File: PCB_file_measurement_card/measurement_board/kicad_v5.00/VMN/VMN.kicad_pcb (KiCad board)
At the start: 2 copper layers, 210.8 x 86.4 mm, 53 parts, among them J1 A/B, J10 Conn_01x08_Female, J11 Conn_01x02_Female, J12 Conn_01x02_Female, J13 Conn_01x08_Female, J2 Screw_Terminal_VMN, J3 Alim DPH5005, J4 Conn_01x08_Female, J5 Conn_01x04_Female, J6 Conn_01x08_Female, J7 Raspberry_Pi_2_3, J8 Conn_02x03_Top_Bottom, J9 Screw_Terminal_01x02, K1 AQY211EH, K2 AQY211EH, K3 AQY211EH, K4 AQY211EH, U1 INA128, U2 MCP23008-xP, U3 LM358, U5 1085-Adress=0X49, U6 1085-Adress=0X48

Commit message: new measurement board
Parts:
- removed Alim_5V_Digital_rasp_iso1540_mcp1, Alim_5V_ina282_iso1: THD_15-1211N, THD_15-1211N:THD151211N
- removed Alim_analog_Vmn1: THD_15-1222N, THD_15-1222N:CONV_THD_15-1222N
- removed J10: Conn_01x08_Female, Connector_PinHeader_2.54mm:PinHeader_1x08_P2.54mm_Vertical
- removed REF** (x8): Hole_3.2mm_M3, MountingHole:MountingHole_3.2mm_M3_ISO7380
- removed U6: 1085-Adress=0X48, 1085:1085
- added ?: , , F.Cu at (247.7, 150.0)
- added ?: , , F.Cu at (247.7, 91.0)
- added ?: , , F.Cu at (203.0, 149.0)
- added ?: , , F.Cu at (202.0, 91.0)
- added Alim_5VA: THD_15-1211N, THD_15-1211N:THD151211N, F.Cu at (166.9, 88.0)
- added Alim_5V_Digital: THD_15-1211N, THD_15-1211N:THD151211N, F.Cu at (190.0, 93.0)
- added Alim_analog_Vmn_measurement_ina128P_lm158: THD_15-1222N, THD_15-1222N:CONV_THD_15-1222N, F.Cu at (85.0, 104.0)
- added D5: BAT86, Diode_THT:D_DO-35_SOD27_P7.62mm_Horizontal, F.Cu at (108.0, 72.2)
- added D6: BAT86, Diode_THT:D_DO-35_SOD27_P7.62mm_Horizontal, F.Cu at (104.0, 79.8)
- added D7: 1N4148, Diode_THT:D_DO-35_SOD27_P7.62mm_Horizontal, F.Cu at (48.0, 67.2)
- added D8: 1N4148, Diode_THT:D_DO-35_SOD27_P7.62mm_Horizontal, F.Cu at (48.0, 79.2)
- added J14: Conn_01x02_Female, Connector_PinHeader_2.54mm:PinHeader_1x02_P2.54mm_Vertical, F.Cu at (86.0, 128.0)
- added J15: Conn_01x08_Female, Connector_PinHeader_2.54mm:PinHeader_1x08_P2.54mm_Vertical, F.Cu at (98.0, 141.0)
- added J16: RX_bat, TerminalBlock_Phoenix:TerminalBlock_Phoenix_MKDS-1,5-2-5.08_1x02_P5.08mm_Horizontal, F.Cu at (189.5, 139.3)
- added K5: AQY212EH, AQY211EH:DIP762W47P254L478H340Q4N, F.Cu at (51.0, 135.0)
- added K6: AQY212EH, AQY211EH:DIP762W47P254L478H340Q4N, F.Cu at (51.0, 141.0)
- added Q1: ZVN4206ASTZ, Package_TO_SOT_THT:TO-92L_Inline, F.Cu at (231.0, 67.0)
- added Q2: ZVN4206ASTZ, Package_TO_SOT_THT:TO-92L_Inline, F.Cu at (208.0, 67.0)
- added R7: 1k, Resistor_THT:R_Axial_DIN0207_L6.3mm_D2.5mm_P7.62mm_Horizontal, F.Cu at (57.2, 142.0)
- added R8: 2, Resistor_THT:R_Axial_DIN0414_L11.9mm_D4.5mm_P20.32mm_Horizontal, F.Cu at (73.0, 142.2)
- added R9: 20 Mohms, Resistor_THT:R_Axial_DIN0204_L3.6mm_D1.6mm_P7.62mm_Horizontal, F.Cu at (44.0, 79.2)
- added U4: 1115-Adress=0X49, 1085:1085, F.Cu at (114.6, 87.4)
- D1, D2: value BAT86 -> 1N4001; footprint Diode_THT:D_DO-35_SOD27_P7.62mm_Horizontal -> Diode_THT:D_DO-41_SOD81_P10.16mm_Horizontal
- J1: value A/B -> DSP_out_12v_GND
- J11: value Conn_01x02_Female -> Screw_Terminal_VMN; footprint Connector_PinHeader_2.54mm:PinHeader_1x02_P2.54mm_Vertical -> TerminalBlock_Phoenix:TerminalBlock_Phoenix_MKDS-1,5-2-5.08_1x02_P5.08mm_Horizontal
- J12: value Conn_01x02_Female -> Conn_01x08_Female; footprint Connector_PinHeader_2.54mm:PinHeader_1x02_P2.54mm_Vertical -> Connector_PinHeader_2.54mm:PinHeader_1x08_P2.54mm_Vertical
- J13: value Conn_01x08_Female -> Conn_01x02_Female; footprint Connector_PinHeader_2.54mm:PinHeader_1x08_P2.54mm_Vertical -> Connector_PinHeader_2.54mm:PinHeader_1x02_P2.54mm_Vertical
- J2: value Screw_Terminal_VMN -> DPS5005_input_0_to_50V
- J3: value Alim DPH5005 -> Screw_Terminal_AB
- J4: moved to F.Cu
- J7: value Raspberry_Pi_2_3 -> Raspberry_Pi_2_3_4; moved to F.Cu
- J8: value Conn_02x03_Top_Bottom -> Connector_I2C_for_mux_or_tools
- J9: value Screw_Terminal_01x02 -> TX_bat; moved to B.Cu
- K1, K2: value AQY211EH -> G5LE-1; footprint AQY211EH:DIP762W47P254L478H340Q4N -> Relay_THT:Relay_SPDT_Omron-G5LE-1
- K3, K4: value AQY211EH -> AQY212EH
- R1, R2: value 1.5k -> 100k
- R6: value 2 -> 1k; footprint Resistor_THT:R_Axial_DIN0414_L11.9mm_D4.5mm_P20.32mm_Horizontal -> Resistor_THT:R_Axial_DIN0207_L6.3mm_D2.5mm_P7.62mm_Horizontal
- U1: value INA128 -> MCP23008-xP; footprint Package_DIP:DIP-8_W7.62mm -> Package_DIP:DIP-18_W7.62mm
- U2: value MCP23008-xP -> INA128; footprint Package_DIP:DIP-18_W7.62mm -> Package_DIP:DIP-8_W7.62mm
- U5: value 1085-Adress=0X49 -> 1115-Adress=0X48
- moved K4 184.9 mm to (51.0, 123.0), turned to 180 degrees
- moved K3 184.5 mm to (51.0, 129.0), turned to 180 degrees
- moved R6 183.2 mm to (57.2, 124.0), turned to 0 degrees
- moved J11 177.2 mm to (37.0, 74.0), turned to -90 degrees
- moved U1 170.1 mm to (216.8, 92.8)
- moved J3 154.9 mm to (36.0, 130.0), turned to -90 degrees
- moved D1 145.2 mm to (220.9, 61.0), turned to 0 degrees
- moved D2 136.3 mm to (197.9, 61.0), turned to 0 degrees
- moved J12 129.5 mm to (98.0, 122.0), turned to 90 degrees
- moved J13 125.4 mm to (86.0, 135.0), turned to 0 degrees
- moved J2 118.3 mm to (171.5, 141.0), turned to 180 degrees
- moved J7 108.4 mm to (249.0, 95.9), turned to 0 degrees
- moved J9 98.4 mm to (187.7, 48.5), turned to 90 degrees
- moved U2 94.2 mm to (60.0, 74.0)
- moved U5 85.8 mm to (180.6, 126.4), turned to -90 degrees
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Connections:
- C1 pad 2: GNDA -> GNDD
- C10 pad 2: -12V -> -12V_A
- C2 pad 2: GNDA -> GNDD
- C3 pad 1: 12V -> +12V_A
- C4 pad 1: -12V -> -12V_A
- C5 pad 1: 12V -> +12V_A
- C6 pad 2: -12V -> -12V_A
- C7 pad 1: 12V -> +12V_A
- C8 pad 1: -12V -> -12V_A
- C9 pad 1: 12V -> +12V_A
- D1 pad 1: 5V -> 5VD
- D2 pad 1: Net-(D1-Pad2) -> 5VD
- D2 pad 2: GNDA -> Net-(D2-Pad2)
- D3 pad 1: 5V -> 5VA
- J1 pad 1: B -> /Relay_switch_dsp/out_12v_DSP
- J1 pad 2: A -> /Relay_switch_dsp/out_GND_DSP
- J11 pad 1: unconnected-(J11-Pad1) -> GNDA
- J11 pad 2: unconnected-(J11-Pad2) -> /Vmn_measurement/Electrode_M
- J12 pad 1: Net-(J3-Pad1) -> AN
- J12 pad 2: Net-(K1-Pad4) -> unconnected-(J12-Pad2)
- J2 pad 1: Net-(J2-Pad1) -> /Current_injection_and_measurement/Input_DSP_+_alim
- J2 pad 2: Net-(J2-Pad2) -> /Current_injection_and_measurement/Input_DSP_GND_alim
- J3 pad 1: Net-(J3-Pad1) -> /Current_injection_and_measurement/A
- J3 pad 2: Net-(J3-Pad2) -> /Current_injection_and_measurement/B
- J5 pad 1: 5V -> 5VA
- J9 pad 1: +12.5V -> +12V_TX_bat
- J9 pad 2: GNDPWR -> GND_TX_bat
- K1 pad 1: Net-(K1-Pad1) -> GND_TX_bat
- K1 pad 2: GNDD -> Net-(D1-Pad2)
- K1 pad 3: B -> /Relay_switch_dsp/out_GND_DSP
- K1 pad 4: Net-(K1-Pad4) -> unconnected-(K1-Pad4)
- K2 pad 1: Net-(K1-Pad1) -> +12V_TX_bat
- K2 pad 2: GNDD -> Net-(D2-Pad2)
- K2 pad 3: A -> /Relay_switch_dsp/out_12v_DSP
- K2 pad 4: Net-(J3-Pad2) -> unconnected-(K2-Pad4)
- K3 pad 3: A -> /Current_injection_and_measurement/B
- K3 pad 4: Net-(K1-Pad4) -> Net-(J14-Pad2)
- K4 pad 3: B -> /Current_injection_and_measurement/A
- K4 pad 4: Net-(J3-Pad2) -> /Current_injection_and_measurement/Input_DSP_+_alim
- R1 pad 1: Net-(K1-Pad1) -> GP2
- R1 pad 2: Net-(R1-Pad2) -> GNDD
- R2 pad 1: Net-(K3-Pad1) -> GP3
- R2 pad 2: Net-(R2-Pad2) -> GNDD
- R4 pad 2: Net-(D3-Pad2) -> Net-(D5-Pad2)
- R5 pad 2: Net-(D1-Pad2) -> Net-(D3-Pad2)
- R6 pad 1: Net-(K1-Pad4) -> Net-(K3-Pad1)
- R6 pad 2: Net-(J3-Pad1) -> GP0
- U1 pad 1: unconnected-(U1-Pad1) -> SCL1
- U1 pad 2: Net-(J2-Pad1) -> SDA1
- U1 pad 3: Net-(J2-Pad2) -> GNDD
- U1 pad 4: -12V -> GNDD
- U1 pad 5: GNDA -> GNDD
- U1 pad 6: Net-(R3-Pad1) -> 5VD
- U1 pad 7: 12V -> unconnected-(U1-Pad7)
- U2 pad 1: SCL1 -> unconnected-(U2-Pad1)
- U2 pad 2: SDA1 -> Net-(R3-Pad1)
- U2 pad 3: GNDD -> /Vmn_measurement/Electrode_M
- U2 pad 4: GNDD -> -12V_A
- U2 pad 5: GNDD -> GNDA
- U2 pad 6: 5VD -> Net-(R3-Pad1)
- U2 pad 7: unconnected-(U2-Pad7) -> +12V_A
- U3 pad 1: Net-(D3-Pad2) -> Net-(D5-Pad2)
- U3 pad 4: -12V -> -12V_A
- U3 pad 7: Net-(D1-Pad2) -> Net-(D3-Pad2)
- U3 pad 8: 12V -> +12V_A
- U5 pad 1: GNDA -> GNDD
- U5 pad 10: 5V -> 5VD
- U5 pad 2: GNDA -> GNDD
- U5 pad 3: GNDA -> GNDD
- U5 pad 6: 5V -> GNDD
- U5 pad 7: SDA2 -> SDA1
- U5 pad 8: SCL2 -> SCL1
- U5 pad 9: GNDA -> GNDD
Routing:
- net GP1: track 0.00 -> 261.6 mm
- net GP0: track 0.00 -> 239.7 mm
- net GND_RX_bat: track 0.00 -> 197.1 mm
- net +12V_RX_bat: track 0.00 -> 192.9 mm
- net 5V: track 167.5 -> 0.00 mm
- net /Current_injection_and_measurement/Input_DSP_+_alim: track 0.00 -> 162.2 mm
- net +12.5V: track 139.2 -> 0.00 mm
- net GNDPWR: track 135.3 -> 0.00 mm
- net 5VD: track 154.9 -> 287.0 mm
- net -12V: track 115.9 -> 0.00 mm
- net /Current_injection_and_measurement/Input_DSP_GND_alim: track 0.00 -> 114.6 mm
- net GNDD: track 110.5 -> 1.08 mm, vias 6 -> 5
- net Net-(J3-Pad1): track 105.1 -> 0.00 mm
- net 5VA: track 0.00 -> 90.1 mm
- net +12V_A: track 0.00 -> 89.9 mm
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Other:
- board size 210.8 x 86.4 mm -> 242 x 126 mm
- board text added: "A"
- board text added: "B"
- board text added: "M"
- board text added: "N"
- board text removed: "+12V GND RX POWER"
- board text removed: "+VDC GND TX POWER"
- board text removed: "B / A"
- board text removed: "M / N"
- board text removed: "OhmPi measurement board v4.00 - OhmPi Team https://reversaal.gitlab.irstea.page/OhmPi"

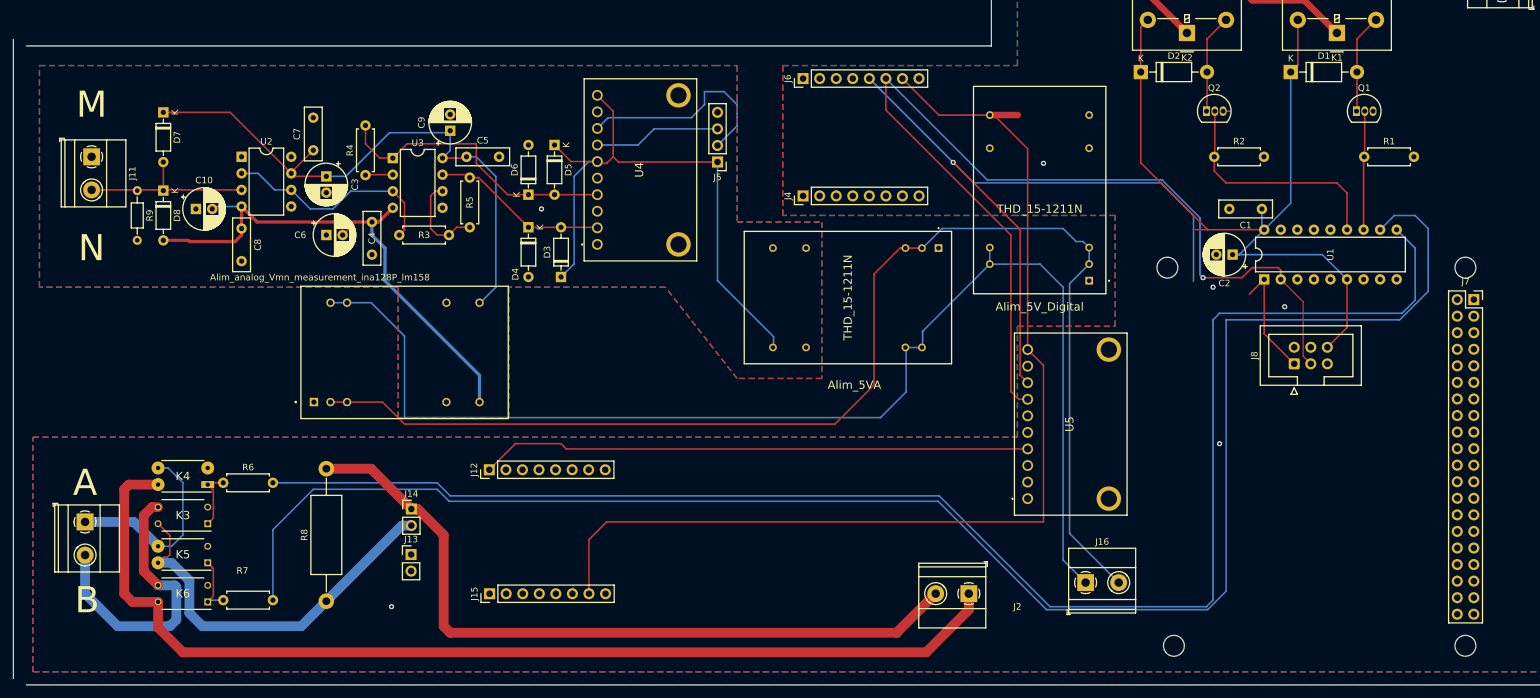
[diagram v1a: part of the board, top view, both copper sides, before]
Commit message: remplacement INA128 par TL082carte maesure
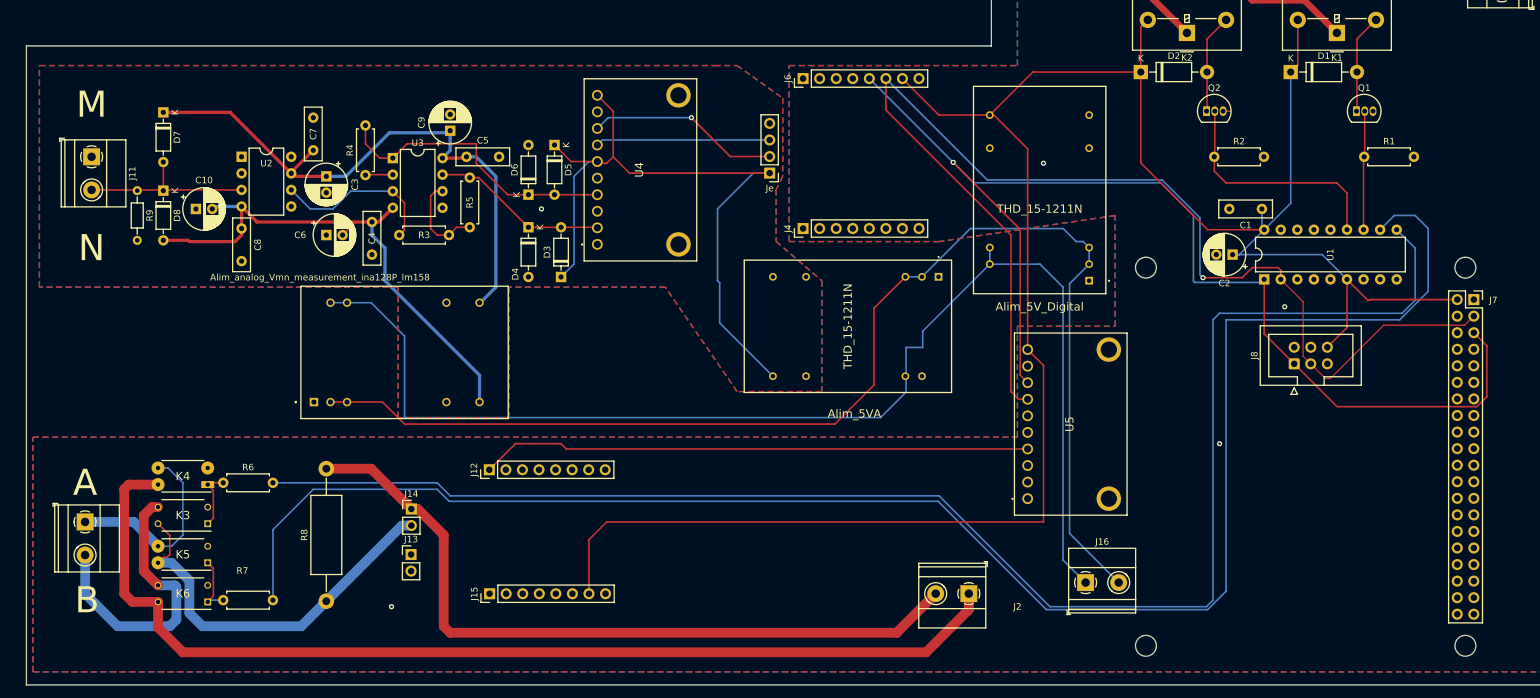
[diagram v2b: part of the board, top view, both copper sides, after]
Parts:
- moved Je 8.18 mm to (141.0, 76.5)
- moved J4 5.00 mm to (146.1, 85.0)
- moved Alim_5VA 4.41 mm to (166.9, 92.4)
- renumbered J5 to Je
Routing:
- net SCL1: track 125.1 -> 176.5 mm
- net 5VD: track 287.0 -> 325.0 mm
- net SDA1: track 154.4 -> 184.3 mm
- net 5VA: track 90.1 -> 106.3 mm
- net Net-(R3-Pad1): track 34.4 -> 25.7 mm
- net SDA2: track 19.5 -> 26.7 mm
- net SCL2: track 33.3 -> 29.6 mm, vias 0 -> 1
- net GND_RX_bat: track 197.1 -> 194.0 mm
- net GNDD: vias 5 -> 4
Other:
- board size 242 x 126 mm -> 240 x 126 mm

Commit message: new version of measurement board
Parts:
- removed Alim_5VA, Alim_5V_Digital: THD_15-1211N, THD_15-1211N:THD151211N
- removed J13: Conn_01x02_Female, Connector_PinHeader_2.54mm:PinHeader_1x02_P2.54mm_Vertical
- removed Je: Conn_01x04_Female, Connector_PinHeader_2.54mm:PinHeader_1x04_P2.54mm_Vertical
- added Alim_5V_Digital_rasp_iso1540_mcp23008_current_7_click1: THD_15-1211N, THD_15-1211N:THD151211N, F.Cu at (190.0, 93.0)
- added Alim_5V_I2C_isolator_Vmn_measurement1: THD_15-1211N, THD_15-1211N:THD151211N, F.Cu at (118.0, 112.0)
- added J5: Conn_01x04_Female, Connector_PinHeader_2.54mm:PinHeader_1x04_P2.54mm_Vertical, F.Cu at (141.0, 78.2)
- J7: value Raspberry_Pi_2_3_4 -> Raspberry_Pi_2_3
- moved J16 131.8 mm to (63.0, 102.0), turned to -90 degrees
- moved J15 7.57 mm to (105.0, 144.0)
- moved J12 7.07 mm to (105.0, 121.0)
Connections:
- U2 pad 2: Net-(R3-Pad1) -> GNDA
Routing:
- net +12V_RX_bat: track 192.9 -> 128.1 mm
- net GND_RX_bat: track 194.0 -> 145.8 mm
- net 5VD: track 325.0 -> 314.4 mm
- net AN: track 84.6 -> 76.5 mm
- net 5VA: track 106.3 -> 100.1 mm
- net /Current_injection_and_measurement/Input_DSP_GND_alim: track 114.6 -> 116.4 mm
- net GNDD: track 1.08 -> 0.00 mm, vias 4 -> 6
- net SCL2: track 29.6 -> 30.3 mm
- net GNDA: vias 1 -> 3
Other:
- board size 240 x 126 mm -> 235 x 124 mm

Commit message: new version of measurement board
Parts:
- J7: moved to B.Cu
- J9: moved to F.Cu
- moved J7 2.50 mm to (246.5, 95.9), turned to 180 degrees
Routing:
- net SCL1: track 176.5 -> 163.5 mm
- net 5VD: track 314.4 -> 319.3 mm
- net SDA1: track 184.3 -> 181.8 mm
- net (no net): vias 0 -> 2
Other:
- board text added: "Ohmpi version 22/11 - https://gitlab.irstea.fr/reversaal/OhmPi"

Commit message: last version of measurement board, with op07
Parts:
- removed U3: LM358, Package_DIP:DIP-8_W7.62mm
- added C11: 100nF, Capacitor_THT:C_Disc_D8.0mm_W2.5mm_P5.00mm, F.Cu at (88.5, 73.0)
- added C12: 10uF, Capacitor_THT:CP_Radial_D6.3mm_P2.50mm, F.Cu at (85.0, 66.0)
- added C13: 100nF, Capacitor_THT:C_Disc_D8.0mm_W2.5mm_P5.00mm, F.Cu at (104.0, 67.5)
- added C14: 10uF, Capacitor_THT:CP_Radial_D6.3mm_P2.50mm, F.Cu at (109.0, 64.0)
- added D10-OHMPI-MEASURE1: LED, LED_THT:LED_D4.0mm, F.Cu at (235.0, 130.0)
- added D11-OHMPI-STACK1: LED, LED_THT:LED_D4.0mm, F.Cu at (229.0, 130.0)
- added D12-LOW-TX-BATTERY1: LED, LED_THT:LED_D4.0mm, F.Cu at (223.0, 130.0)
- added D9-OHMPI-RUN-WAITING1: LED, LED_THT:LED_D4.0mm, F.Cu at (241.0, 130.0)
- added J10: DSP+, Connector_PinHeader_2.54mm:PinHeader_1x01_P2.54mm_Vertical, F.Cu at (177.0, 141.0)
- added J17: DSP GND, Connector_PinHeader_2.54mm:PinHeader_1x01_P2.54mm_Vertical, F.Cu at (86.0, 121.0)
- added J18: Conn_01x01, Connector_PinHeader_2.54mm:PinHeader_1x01_P2.54mm_Vertical, F.Cu at (37.0, 85.0)
- added J19: Conn_01x01, Connector_PinHeader_2.54mm:PinHeader_1x01_P2.54mm_Vertical, F.Cu at (37.0, 68.0)
- added J20: shunt +, Connector_PinHeader_2.54mm:PinHeader_1x01_P2.54mm_Vertical, F.Cu at (86.0, 136.0)
- added J21: shunt -, Connector_PinHeader_2.54mm:PinHeader_1x01_P2.54mm_Vertical, F.Cu at (160.0, 141.0)
- added R10: 330, Resistor_THT:R_Axial_DIN0207_L6.3mm_D2.5mm_P7.62mm_Horizontal, F.Cu at (241.0, 116.2)
- added R11: 330, Resistor_THT:R_Axial_DIN0207_L6.3mm_D2.5mm_P7.62mm_Horizontal, F.Cu at (235.0, 116.2)
- added R12: 330, Resistor_THT:R_Axial_DIN0207_L6.3mm_D2.5mm_P7.62mm_Horizontal, F.Cu at (229.0, 116.0)
- added R13: 330, Resistor_THT:R_Axial_DIN0207_L6.3mm_D2.5mm_P7.62mm_Horizontal, F.Cu at (223.0, 116.0)
- added RV1: R_Potentiometer, Potentiometer_THT:Potentiometer_Bourns_3296W_Vertical, F.Cu at (66.0, 66.0)
- added RV2: R_Potentiometer, Potentiometer_THT:Potentiometer_Bourns_3296W_Vertical, F.Cu at (98.5, 60.0)
- added RV3: R_Potentiometer, Potentiometer_THT:Potentiometer_Bourns_3296W_Vertical, F.Cu at (98.0, 78.0)
- added U6: OP07, Package_DIP:DIP-8_W7.62mm, F.Cu at (92.2, 65.2)
- added U7: OP07, Package_DIP:DIP-8_W7.62mm, F.Cu at (92.2, 83.2)
- D7, D8: value 1N4148 -> BAT86
- U2: value INA128 -> OP07
- moved C7 34.4 mm to (103.0, 85.5), turned to 0 degrees
- moved C8 29.5 mm to (89.0, 90.5), turned to 90 degrees
- moved R4 24.0 mm to (103.0, 78.0)
- moved C5 21.0 mm to (73.5, 73.0)
- moved C4 20.1 mm to (60.0, 85.5)
- moved C9 19.8 mm to (108.0, 81.6)
- moved R5 14.9 mm to (105.0, 95.8)
- moved C6 11.2 mm to (84.0, 88.0), turned to -90 degrees
- moved D4 10.5 mm to (113.0, 79.4)
- moved D6 10.5 mm to (113.0, 74.4)
- moved D5 10.5 mm to (117.0, 66.8)
- moved D3 9.67 mm to (117.0, 87.0)
- moved U4 8.00 mm to (122.6, 87.4)
- moved R3 7.07 mm to (79.2, 81.0)
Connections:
- R3 pad 1: Net-(R3-Pad1) -> Net-(U6-Pad3)
- U1 pad 14: unconnected-(U1-Pad14) -> GP4
- U1 pad 15: unconnected-(U1-Pad15) -> GP5
- U1 pad 16: unconnected-(U1-Pad16) -> GP6
- U1 pad 17: unconnected-(U1-Pad17) -> GP7
- U2 pad 1: unconnected-(U2-Pad1) -> Net-(U2-Pad1)
- U2 pad 2: GNDA -> Net-(U6-Pad3)
- U2 pad 5: GNDA -> unconnected-(U2-Pad5)
- U2 pad 6: Net-(R3-Pad1) -> Net-(U6-Pad3)
- U2 pad 8: unconnected-(U2-Pad8) -> Net-(U2-Pad8)
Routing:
- net GP7: track 0.00 -> 84.7 mm
- net GP6: track 0.00 -> 73.7 mm
- net GP5: track 0.00 -> 62.8 mm
- net GP4: track 0.00 -> 50.6 mm
- net +12V_A: track 89.9 -> 131.8 mm
- net Net-(U6-Pad3): track 0.00 -> 40.6 mm
- net -12V_A: track 86.4 -> 114.6 mm
- net Net-(R3-Pad1): track 25.7 -> 0.00 mm
- net Net-(D5-Pad2): track 45.2 -> 26.6 mm
- net /Current_injection_and_measurement/Input_DSP_GND_alim: track 116.4 -> 129.9 mm
- net Net-(U6-Pad2): track 4.23 -> 15.8 mm
- net Net-(R3-Pad2): track 14.0 -> 24.3 mm
- net SCL2: track 30.3 -> 20.9 mm
- net Net-(U2-Pad8): track 0.00 -> 8.67 mm
- net Net-(U2-Pad1): track 0.00 -> 8.38 mm
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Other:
- outline, holes or cut-outs redrawn
- board text added: "+12V"
- board text added: "DSP GND"
- board text added: "DSP+"
- board text added: "GND"
- board text added: "RX"
